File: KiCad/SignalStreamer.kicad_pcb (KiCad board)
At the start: 2 copper layers, 100.3 x 59.1 mm, 49 parts, among them J105 Conn_01x02, T101 Coupled_Inductors_2

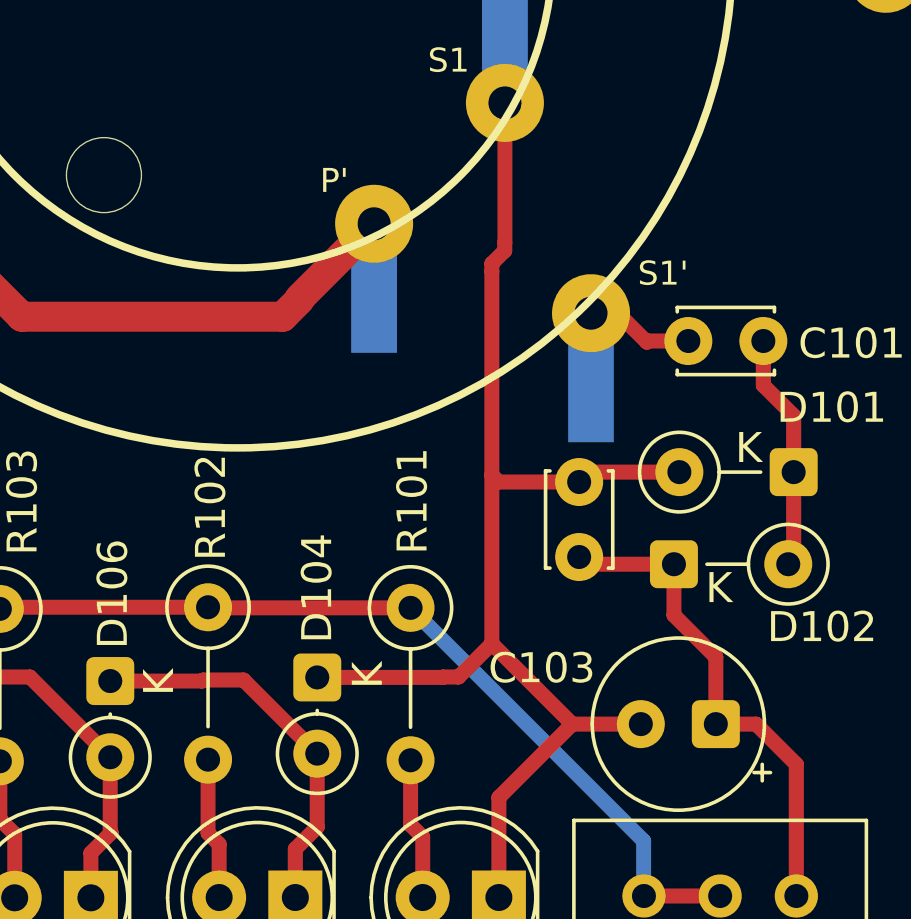
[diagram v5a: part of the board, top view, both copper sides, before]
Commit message: PCB
Minor changes to improve clearances
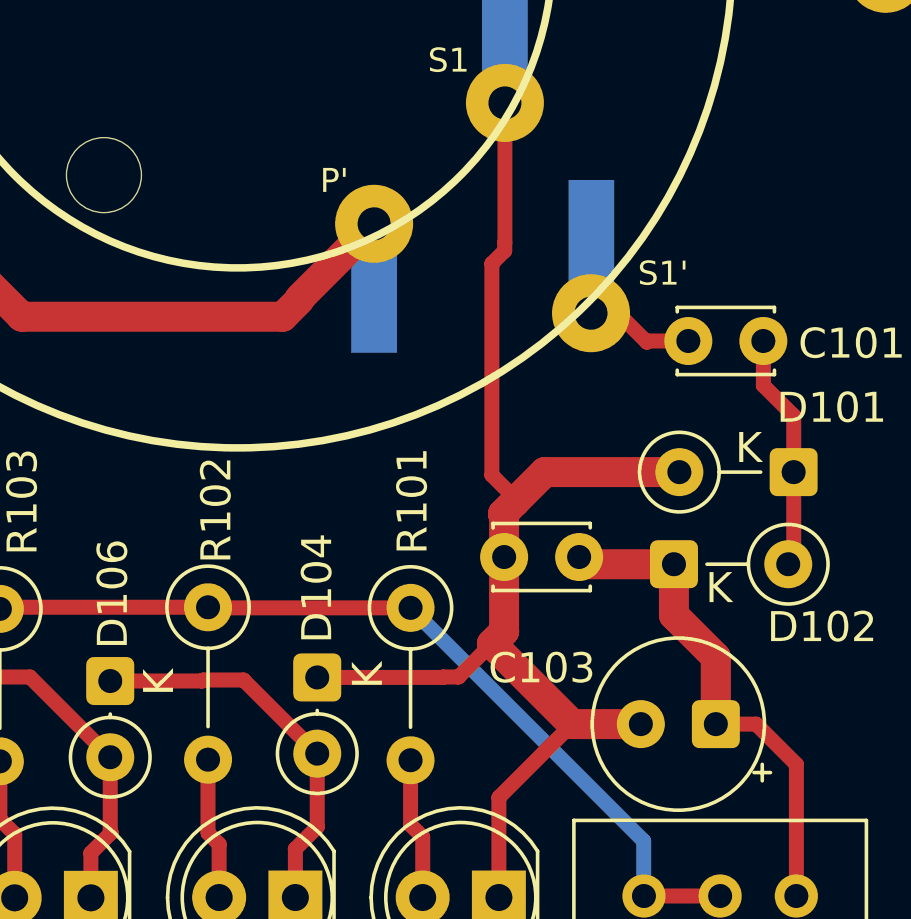
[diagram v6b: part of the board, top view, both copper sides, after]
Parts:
- turned C102 to 180 degrees
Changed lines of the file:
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@@
 		)
 		(pad "2" smd rect
-			(at 11.78 13.81)
+			(at 11.79 10.07)
 			(size 1.524 5)
 			(layers "B.Cu" "B.Mask" "B.Paste")
@@
 	(footprint "Capacitor_THT:C_Disc_D3.0mm_W2.0mm_P2.50mm"
 		(layer "F.Cu")
-		(at 91.01 99 90)
+		(at 91.01 99 180)
 		(descr "C, Disc series, Radial, pin pitch=2.50mm, diameter*width=3*2mm^2, Capacitor")
 		(tags "C Disc series Radial pin pitch 2.50mm diameter 3mm width 2mm Capacitor")
 		(property "Reference" "C102"
-			(at 1.25 -2.25 90)
+			(at 1.25 -2.25 0)
 			(layer "F.SilkS")
 			(hide yes)
@@
 		)
 		(property "Value" "470nF"
-			(at 1.25 2.25 90)
+			(at 1.25 2.25 0)
 			(layer "F.Fab")
 			(hide yes)
@@
 		)
 		(property "Datasheet" "https://product.tdk.com/en/system/files/dam/doc/product/capacitor/ceramic/lead-mlcc/catalog/leadmlcc_halogenfree_fa_en.pdf"
-			(at 0 0 90)
+			(at 0 0 0)
 			(layer "F.Fab")
 			(hide yes)
@@
 		)
 		(property "Description" "CAP CER 0.47UF 100V X7S RADIAL"
-			(at 0 0 90)
+			(at 0 0 0)
 			(layer "F.Fab")
 			(hide yes)
@@
 		)
 		(property "Digi-Key Part No." "445-180414-1-ND "
-			(at 0 0 90)
+			(at 0 0 180)
 			(unlocked yes)
 			(layer "F.Fab")
@@
 		)
 		(property "Manufacturer" "TDK Corporation"
-			(at 0 0 90)
+			(at 0 0 180)
 			(unlocked yes)
 			(layer "F.Fab")
@@
 		)
 		(property "Manufacturer PN" "FA14X7S2A474KRU06"
-			(at 0 0 90)
+			(at 0 0 180)
 			(unlocked yes)
 			(layer "F.Fab")
@@
 		)
 		(property "Link" "https://www.digikey.com/en/products/detail/tdk-corporation/FA14X7S2A474KRU06/5865817"
-			(at 0 0 90)
+			(at 0 0 180)
 			(unlocked yes)
 			(layer "F.Fab")
@@
 		)
 		(property "Sim.Enable" ""
-			(at 0 0 90)
+			(at 0 0 180)
 			(unlocked yes)
 			(layer "F.Fab")
@@
 		(attr through_hole)
 		(fp_line
-			(start 2.87 -1.12)
-			(end 2.87 -0.972)
+			(start 2.87 1.12)
+			(end -0.37 1.12)
 			(stroke
 				(width 0.12)
@@
 		)
 		(fp_line
-			(start -0.37 -1.12)
-			(end 2.87 -1.12)
+			(start 2.87 0.972)
+			(end 2.87 1.12)
 			(stroke
 				(width 0.12)
@@
 		)
 		(fp_line
-			(start -0.37 -0.972)
-			(end -0.37 -1.12)
+			(start 2.87 -1.12)
+			(end 2.87 -0.972)
 			(stroke
 				(width 0.12)
@@
 		)
 		(fp_line
-			(start 2.87 0.972)
-			(end 2.87 1.12)
+			(start -0.37 1.12)
+			(end -0.37 0.972)
 			(stroke
 				(width 0.12)
@@
 		)
 		(fp_line
-			(start 2.87 1.12)
-			(end -0.37 1.12)
+			(start -0.37 -0.972)
+			(end -0.37 -1.12)
 			(stroke
 				(width 0.12)
@@
 		)
 		(fp_line
-			(start -0.37 1.12)
-			(end -0.37 0.972)
+			(start -0.37 -1.12)
+			(end 2.87 -1.12)
 			(stroke
 				(width 0.12)
@@
 		)
 		(fp_text user "${REFERENCE}"
-			(at 1.25 0 90)
+			(at 1.25 0 0)
 			(layer "F.Fab")
 			(effects
@@
 		)
 		(pad "1" thru_hole circle
-			(at 0 0 90)
+			(at 0 0 180)
 			(size 1.6 1.6)
 			(drill 0.8)
@@
 		)
 		(pad "2" thru_hole circle
-			(at 2.5 0 90)
+			(at 2.5 0 180)
 			(size 1.6 1.6)
 			(drill 0.8)
@@
 		(tags "Resistor Axial_DIN0207 series Axial Vertical pin pitch 5.08mm 0.25W = 1/4W length 6.3mm diameter 2.5mm")
 		(property "Reference" "R102"
-			(at -3.335 -0.1 90)
+			(at -3.245 -0.28 90)
 			(layer "F.SilkS")
 			(effects
@@
 		(start 94.17 100.94)
 		(end 95.566369 102.336369)
-		(width 0.5)
+		(width 1)
 		(layer "F.Cu")
 		(net 3)
@@
 		(start 95.566369 102.336369)
 		(end 95.566369 104.57)
-		(width 0.5)
+		(width 1)
 		(layer "F.Cu")
 		(net 3)
@@
 		(start 94.17 99.24)
 		(end 91.25 99.24)
-		(width 0.5)
+		(width 1)
 		(layer "F.Cu")
 		(net 3)
@@
 		(start 94.17 99.24)
 		(end 94.17 100.94)
-		(width 0.5)
+		(width 1)
 		(layer "F.Cu")
 		(net 3)
@@
 	)
 	(segment
+		(start 88.1 89.22)
+		(end 88.1 96.27)
+		(width 0.5)
+		(layer "F.Cu")
+		(net 5)
+	)
+	(segment
+		(start 88.51 99)
+		(end 88.51 101.48)
+		(width 1)
+		(layer "F.Cu")
+		(net 5)
+	)
+	(segment
 		(start 90.78 104.57)
 		(end 88.1 101.89)
+		(width 1)
+		(layer "F.Cu")
+		(net 5)
+	)
+	(segment
+		(start 88.1 96.27)
+		(end 88.87 97.04)
 		(width 0.5)
 		(layer "F.Cu")
@@
 	)
 	(segment
+		(start 88.87 97.16)
+		(end 88.47 97.56)
+		(width 1)
+		(layer "F.Cu")
+		(net 5)
+	)
+	(segment
+		(start 89.86 96.17)
+		(end 88.87 97.16)
+		(width 1)
+		(layer "F.Cu")
+		(net 5)
+	)
+	(segment
 		(start 88.1 101.89)
 		(end 86.99 103)
@@
 	)
 	(segment
-		(start 88.1 89.48)
-		(end 88.1 89.22)
-		(width 0.5)
+		(start 88.51 97.6)
+		(end 88.51 99)
+		(width 1)
 		(layer "F.Cu")
 		(net 5)
@@
 	)
 	(segment
-		(start 88.1 101.89)
-		(end 88.1 96.27)
+		(start 88.53 88.79)
+		(end 88.1 89.22)
 		(width 0.5)
 		(layer "F.Cu")
@@
 	)
 	(segment
-		(start 91.01 96.5)
-		(end 88.33 96.5)
+		(start 88.53 88.5218)
+		(end 88.53 88.79)
 		(width 0.5)
 		(layer "F.Cu")
@@
 	)
 	(segment
-		(start 86.47 103)
-		(end 86.455685 103.014315)
-		(width 0.5)
+		(start 94.350686 96.17)
+		(end 89.86 96.17)
+		(width 1)
 		(layer "F.Cu")
 		(net 5)
 	)
 	(segment
-		(start 91.34 96.17)
-		(end 91.01 96.5)
+		(start 86.47 103)
+		(end 86.455685 103.014315)
 		(width 0.5)
 		(layer "F.Cu")
@@
 	)
 	(segment
-		(start 88.1 96.27)
-		(end 88.1 89.48)
+		(start 88.87 97.04)
+		(end 88.87 97.16)
 		(width 0.5)
 		(layer "F.Cu")
@@
 	)
 	(segment
-		(start 88.1 89.22)
-		(end 88.53 88.79)
-		(width 0.5)
+		(start 88.47 97.56)
+		(end 88.51 97.6)
+		(width 1)
 		(layer "F.Cu")
 		(net 5)
@@
 		(start 93.066369 104.57)
 		(end 90.78 104.57)
-		(width 0.5)
-		(layer "F.Cu")
-		(net 5)
-	)
-	(segment
-		(start 88.53 88.79)
-		(end 88.53 88.5218)
-		(width 0.5)
+		(width 1)
 		(layer "F.Cu")
 		(net 5)
@@
 	)
 	(segment
-		(start 94.350686 96.17)
-		(end 91.34 96.17)
-		(width 0.5)
-		(layer "F.Cu")
-		(net 5)
-	)
-	(segment
-		(start 88.33 96.5)
-		(end 88.1 96.27)
-		(width 0.5)
+		(start 88.51 101.48)
+		(end 88.1 101.89)
+		(width 1)
 		(layer "F.Cu")
 		(net 5)

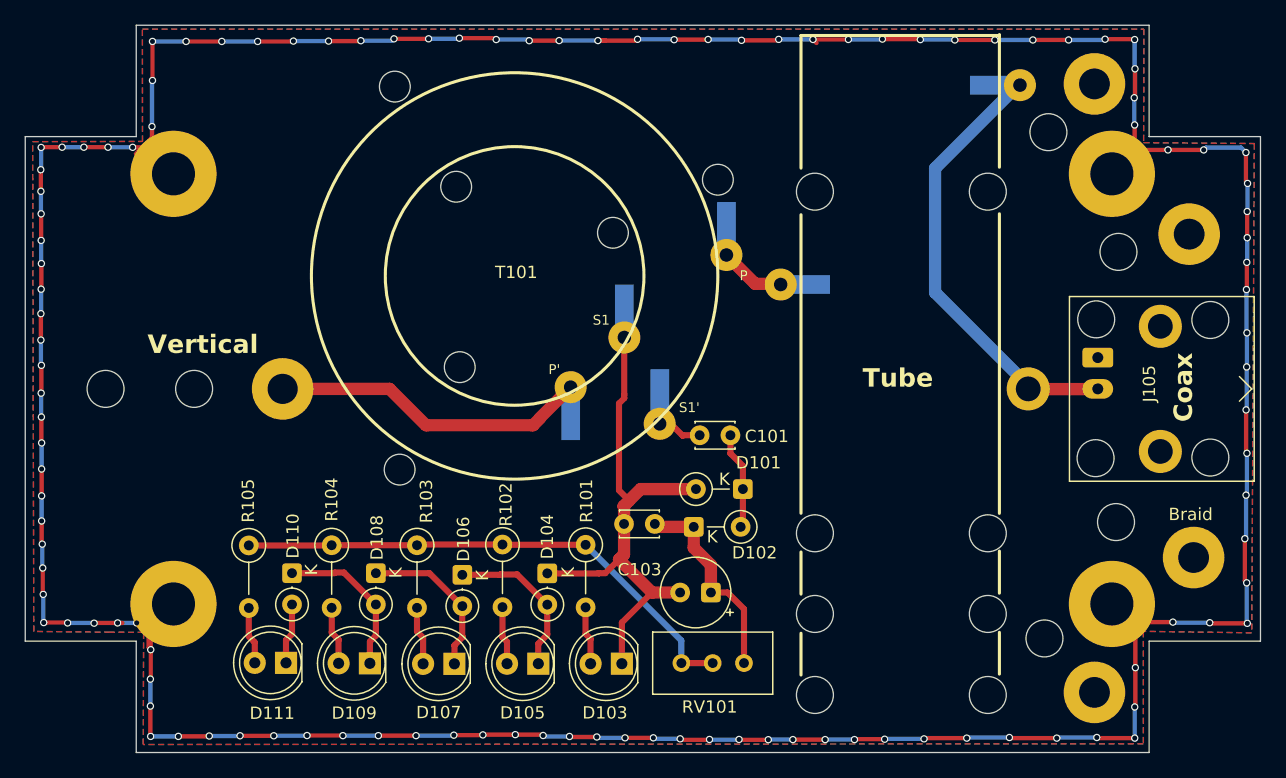
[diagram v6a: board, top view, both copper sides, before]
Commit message: PCB
Minor PCB tweaks
Removes all DRC warnings
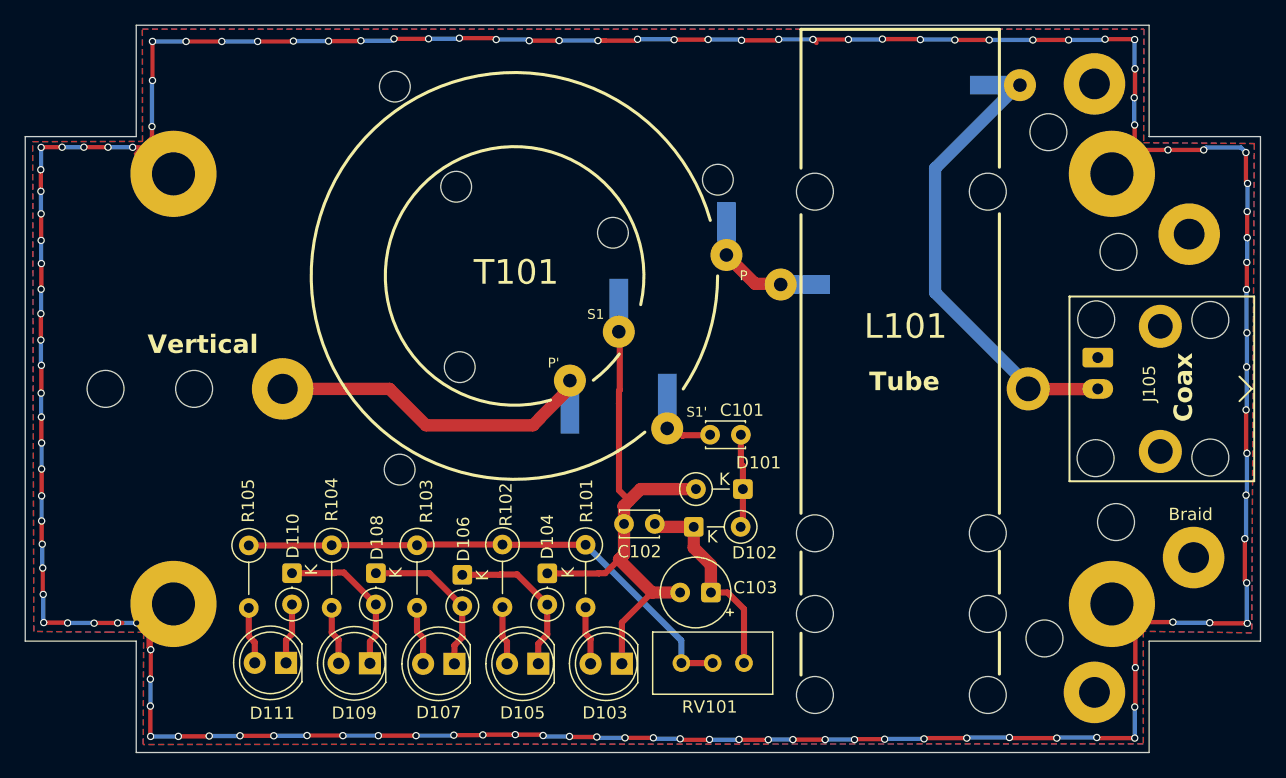
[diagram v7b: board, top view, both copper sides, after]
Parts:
- moved C101 0.85 mm to (98.0, 91.8)
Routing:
- net GND: track 331.4 -> 314.0 mm
- net Net-(AE101-A): track 27.3 -> 26.3 mm
- net Net-(J105-Pin_1): track 36.2 -> 35.5 mm
- net Net-(T101-IN+): track 3.66 -> 3.05 mm
- net Net-(D101-K): track 7.93 -> 7.33 mm
